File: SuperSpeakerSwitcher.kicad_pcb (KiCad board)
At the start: 2 copper layers, 109 x 177 mm, 57 parts, among them J1 Conn_01x02, J10 Conn_01x01, J11 Conn_01x01, J12 Conn_01x01, J13 Conn_01x01, J14 Conn_01x01, J15 Conn_01x01, J16 Conn_01x01, J17 Conn_01x01, J18 Conn_01x01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

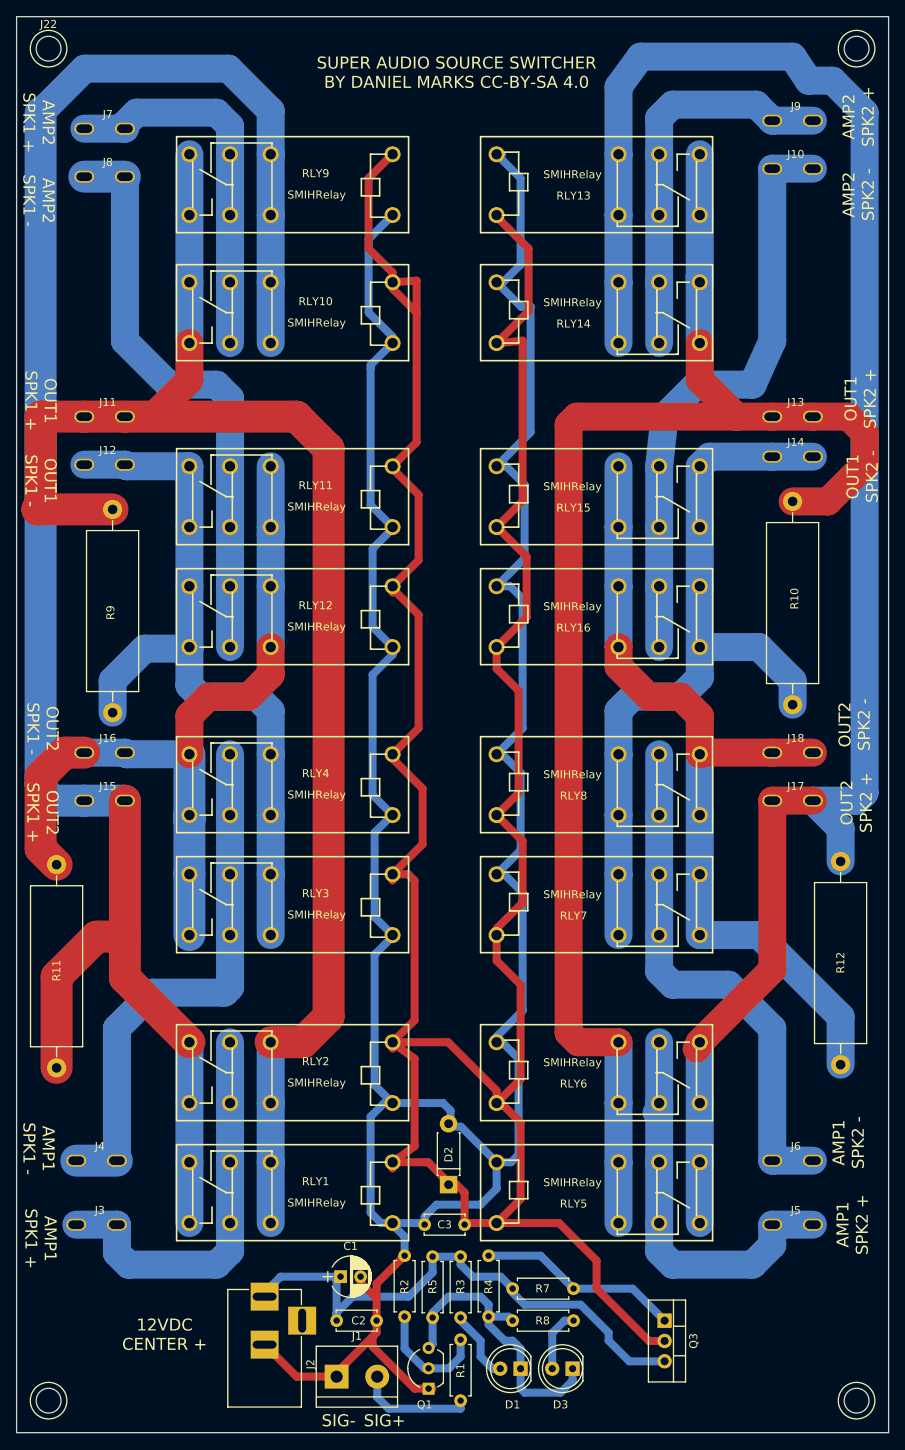
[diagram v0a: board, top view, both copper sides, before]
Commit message: Bulked up the traces
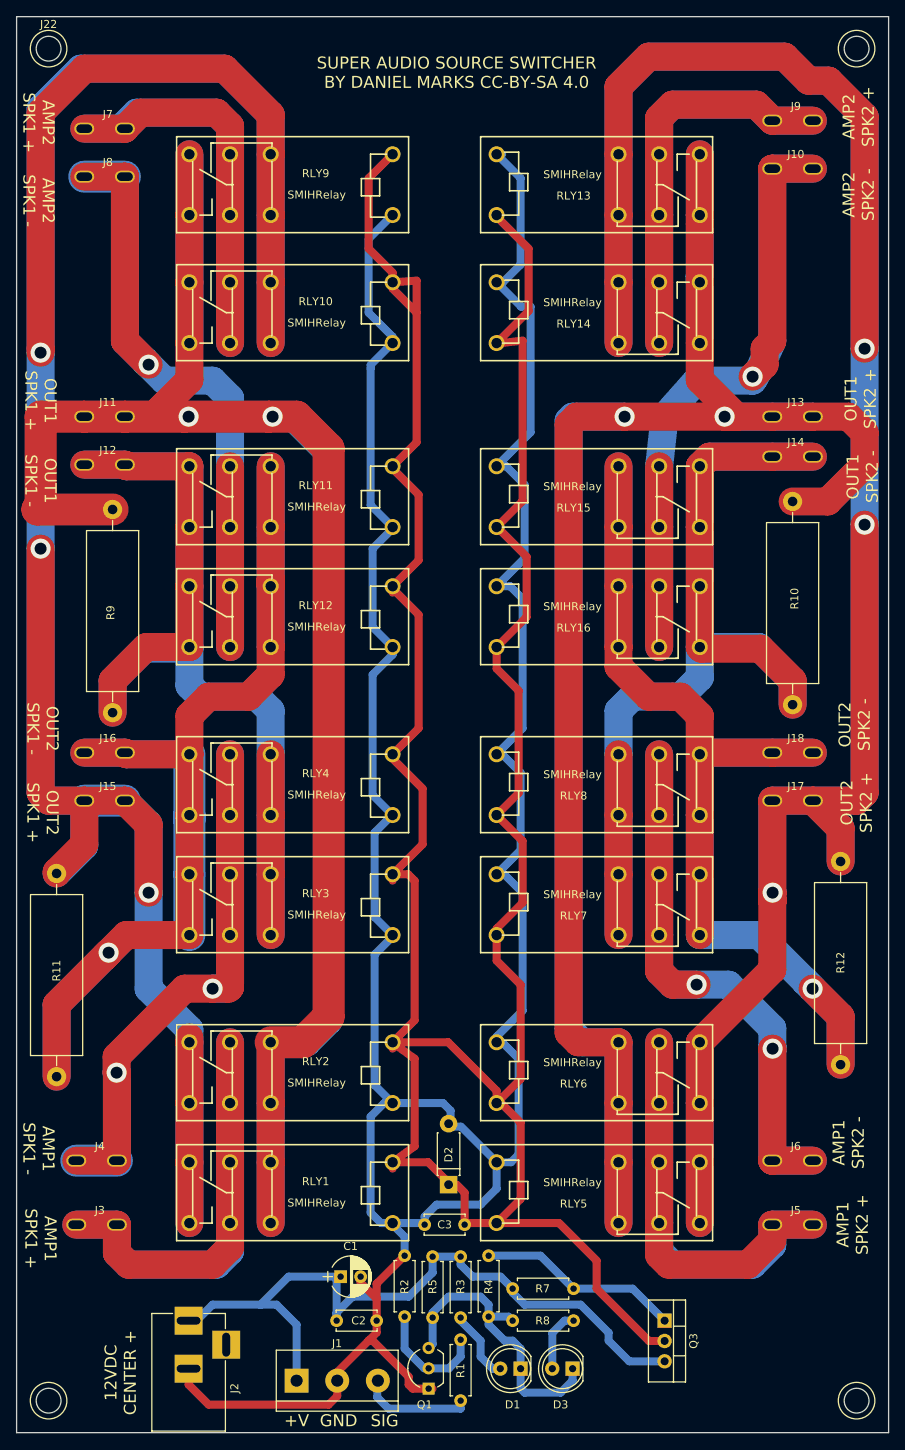
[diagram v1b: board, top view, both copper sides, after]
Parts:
- J1: value Conn_01x02 -> Conn_01x03; footprint Connectors_Terminal_Blocks:TerminalBlock_bornier-2_P5.08mm -> Connectors_Terminal_Blocks:TerminalBlock_bornier-3_P5.08mm
- moved R11 26.5 mm to (23.0, 144.5), turned to 90 degrees
- moved J2 9.96 mm to (39.5, 175.0)
- moved J1 5.02 mm to (53.0, 182.5)
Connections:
- J1 pad 1: GND -> +12V
- J1 pad 2: Net-(J1-Pad2) -> GND
- R1 pad 1: Net-(J1-Pad2) -> Net-(J1-Pad3)
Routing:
- net OUT2SPK2POS: track 231.4 -> 415.8 mm, vias 0 -> 3
- net OUT2SPK1POS: track 236.2 -> 404.8 mm, vias 0 -> 3
- net OUT1SPK2POS: track 194.8 -> 343.7 mm, vias 0 -> 2
- net OUT1SPK1POS: track 199.2 -> 347.6 mm, vias 0 -> 2
- net OUT2SPK1NEG: track 98.7 -> 188.6 mm, vias 0 -> 1
- net OUT1SPK2NEG: track 97.3 -> 173.5 mm
- net OUT1SPK1NEG: track 95.6 -> 169.4 mm
- net OUT2SPK2NEG: track 107.2 -> 179.0 mm, vias 0 -> 1
- net AMP2SPK2NEG: track 74.1 -> 129.1 mm, vias 0 -> 1
- net AMP2SPK1NEG: track 72.8 -> 126.0 mm, vias 0 -> 1
- net AMP1SPK2NEG: track 65.8 -> 117.6 mm, vias 0 -> 2
- net AMP1SPK1POS: track 50.2 -> 100.1 mm
- net AMP2SPK2POS: track 48.9 -> 97.7 mm
- net AMP1SPK2POS: track 50.9 -> 99.1 mm
- net AMP2SPK1POS: track 47.2 -> 94.1 mm
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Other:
- board text added: "+V"
- board text added: "GND"
- board text added: "SIG"
- board text removed: "SIG+"
- board text removed: "SIG-"

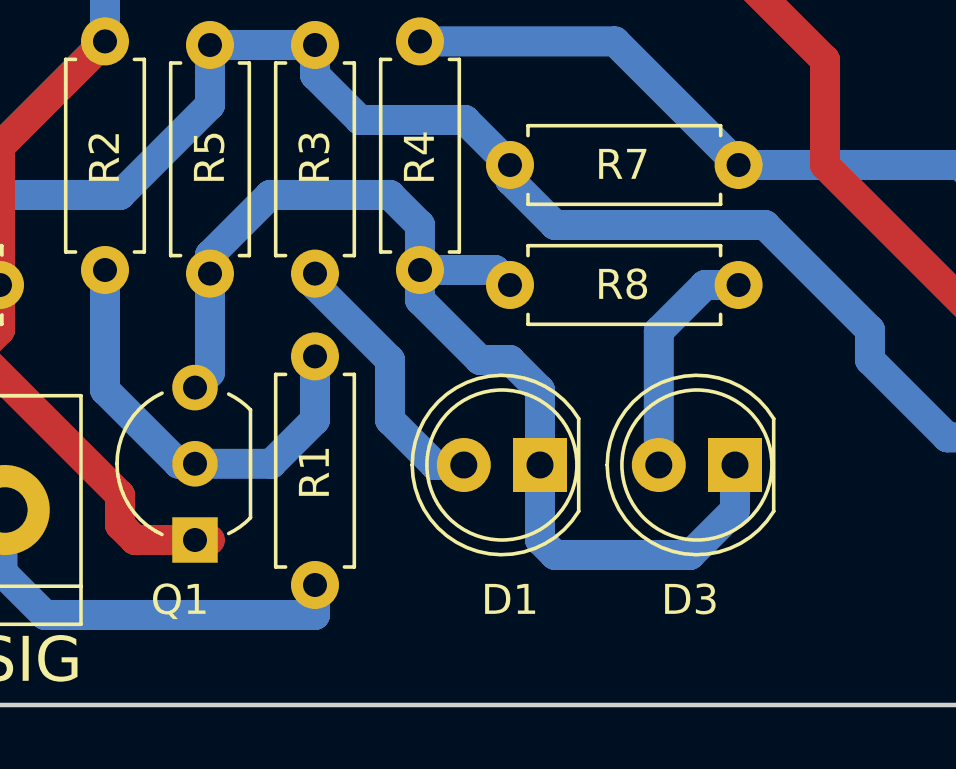
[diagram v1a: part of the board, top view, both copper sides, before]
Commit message: Fixed on and off diodes
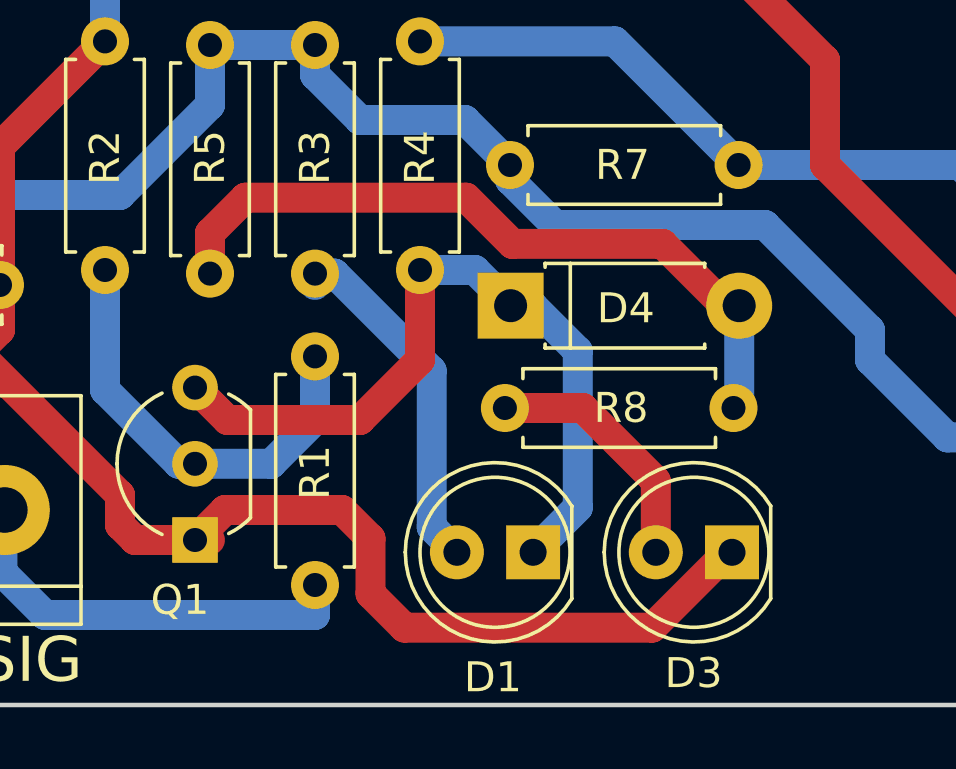
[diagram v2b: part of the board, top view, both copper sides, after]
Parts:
- added D4: 1N4007, Diodes_THT:D_DO-41_SOD81_P7.62mm_Horizontal, F.Cu at (80.0, 175.7)
- moved R8 8.50 mm to (87.5, 179.1), turned to 180 degrees
- moved D1 2.92 mm to (80.8, 183.9)
- moved D3 2.91 mm to (87.4, 183.9)
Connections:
- D3 pad 1: Net-(D1-Pad1) -> GND
- R5 pad 2: Net-(D1-Pad1) -> Net-(D4-Pad2)
- R8 pad 1: Net-(D1-Pad1) -> Net-(D4-Pad2)
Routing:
- net Net-(D4-Pad2): track 0.00 -> 24.8 mm
- net GND: track 393.8 -> 415.8 mm
- net Net-(D1-Pad1): track 37.9 -> 25.7 mm
- net Net-(D1-Pad2): track 9.00 -> 12.1 mm
- net Net-(D3-Pad2): track 7.76 -> 8.42 mm
